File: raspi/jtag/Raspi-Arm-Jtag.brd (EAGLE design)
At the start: 67 x 36.8 mm, 2 parts

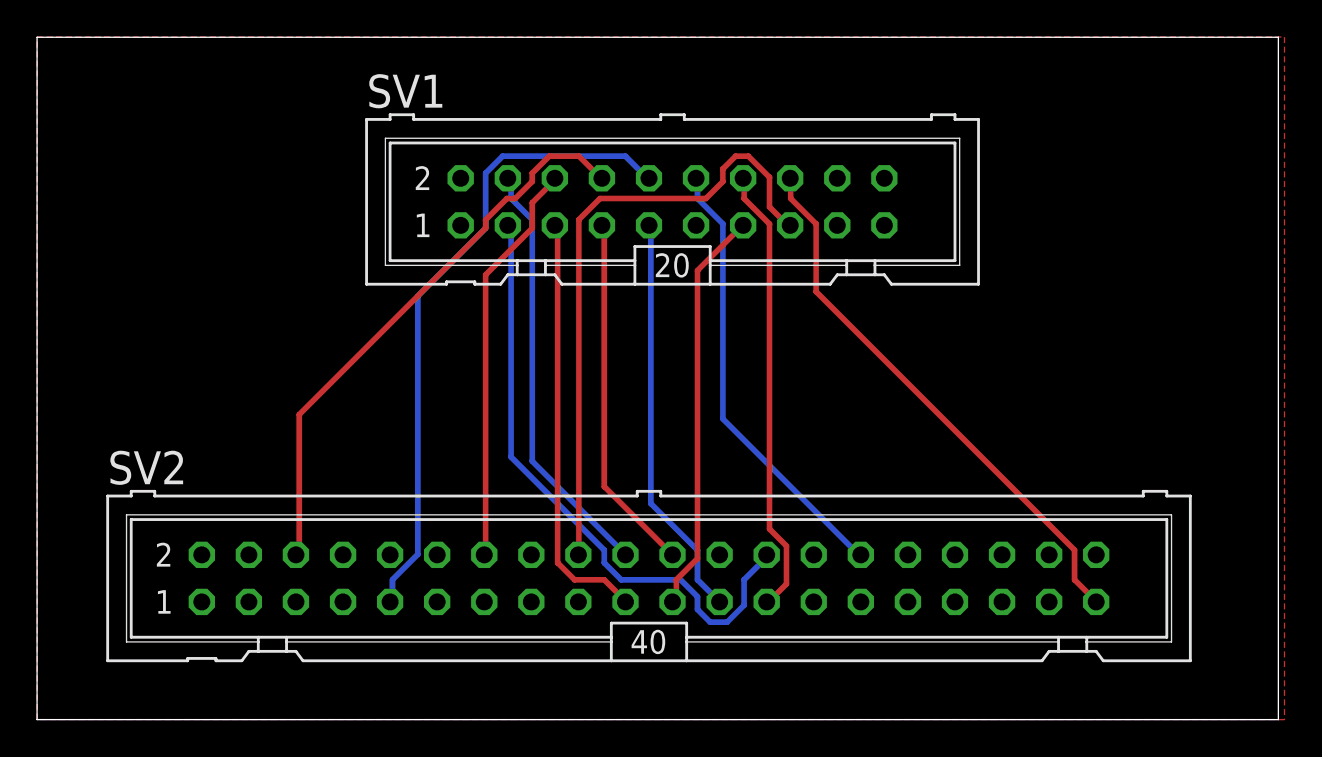
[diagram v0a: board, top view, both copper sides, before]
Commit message: Raspi: Neue Adapter-Schaltpläne
git-svn-id: https://cvsvn/svn/raspi/trunk@92 50237d99-7d21-444e-87dd-016511c29f8c
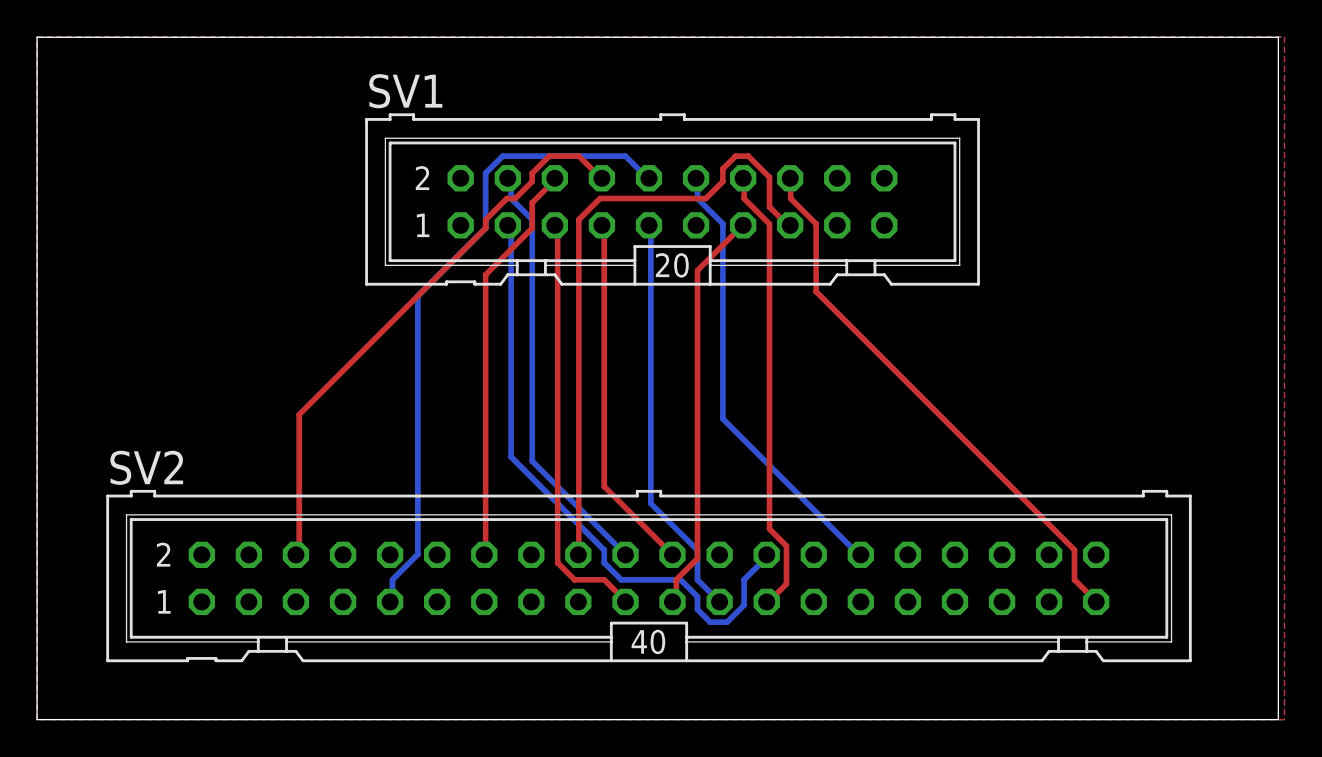
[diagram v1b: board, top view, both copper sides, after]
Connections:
- removed net N$10: SV1.4, SV2.20
- removed net N$11: SV1.10, SV2.9
- removed net N$12: SV1.14, SV2.25
- removed net N$13: SV1.16, SV2.39
- removed net N$7: SV1.6, SV2.14
- removed net N$8: SV1.8, SV2.6
- removed net N$9: SV1.12, SV2.30
- new net GND: SV1.10, SV1.12, SV1.14, SV1.16, SV1.4, SV1.6, SV1.8, SV2.14, SV2.20, SV2.25, SV2.30, SV2.39, SV2.6, SV2.9
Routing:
- net GND: track 0.00 -> 188.7 mm
- net N$11: track 35.0 -> 0.00 mm
- net N$8: track 30.9 -> 0.00 mm
- net N$13: track 29.7 -> 0.00 mm
- net N$12: track 24.3 -> 0.00 mm
- net N$9: track 24.0 -> 0.00 mm
- net N$10: track 23.0 -> 0.00 mm
- net N$7: track 21.9 -> 0.00 mm
- added copper zone on layer 1, net GND
- added copper zone on layer 16, net GND
- removed copper zone on layer 1, net GNG
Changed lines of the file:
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@@
 <wire x1="42.9768" y1="26.7462" x2="43.18" y2="26.67" width="0.3048" layer="1"/>
 </signal>
-<signal name="N$10">
-<contactref element="SV2" pad="20"/>
-<contactref element="SV1" pad="4"/>
-<wire x1="28.1178" y1="28.1178" x2="28.1178" y2="29.0322" width="0.3048" layer="16"/>
-<wire x1="29.2608" y1="26.9748" x2="28.1178" y2="28.1178" width="0.3048" layer="16"/>
-<wire x1="29.2608" y1="13.9446" x2="29.2608" y2="26.9748" width="0.3048" layer="16"/>
-<wire x1="34.29" y1="8.9154" x2="29.2608" y2="13.9446" width="0.3048" layer="16"/>
-<wire x1="28.1178" y1="29.0322" x2="27.94" y2="29.21" width="0.3048" layer="16"/>
-<wire x1="34.29" y1="8.9154" x2="34.29" y2="8.89" width="0.3048" layer="16"/>
-</signal>
-<signal name="N$7">
-<contactref element="SV2" pad="14"/>
-<contactref element="SV1" pad="6"/>
-<wire x1="26.7462" y1="24.003" x2="26.7462" y2="8.9154" width="0.3048" layer="1"/>
-<wire x1="29.2608" y1="26.5176" x2="26.7462" y2="24.003" width="0.3048" layer="1"/>
-<wire x1="29.2608" y1="27.8892" x2="29.2608" y2="26.5176" width="0.3048" layer="1"/>
-<wire x1="30.4038" y1="29.0322" x2="29.2608" y2="27.8892" width="0.3048" layer="1"/>
-<wire x1="26.7462" y1="8.9154" x2="26.67" y2="8.89" width="0.3048" layer="1"/>
-<wire x1="30.4038" y1="29.0322" x2="30.48" y2="29.21" width="0.3048" layer="1"/>
-</signal>
-<signal name="N$8">
+<signal name="GND">
+<polygon width="0.1524" layer="1" isolate="0.8128">
+<vertex x="2.54" y="36.83"/>
+<vertex x="69.85" y="36.83"/>
+<vertex x="69.85" y="0"/>
+<vertex x="2.54" y="0"/>
+</polygon>
+<contactref element="SV2" pad="25"/>
+<contactref element="SV1" pad="14"/>
+<wire x1="40.6908" y1="28.1178" x2="40.6908" y2="29.0322" width="0.3048" layer="1"/>
+<wire x1="42.0624" y1="26.7462" x2="40.6908" y2="28.1178" width="0.3048" layer="1"/>
+<wire x1="42.0624" y1="10.287" x2="42.0624" y2="26.7462" width="0.3048" layer="1"/>
+<wire x1="42.9768" y1="9.3726" x2="42.0624" y2="10.287" width="0.3048" layer="1"/>
+<wire x1="42.9768" y1="7.3152" x2="42.9768" y2="9.3726" width="0.3048" layer="1"/>
+<wire x1="42.0624" y1="6.4008" x2="42.9768" y2="7.3152" width="0.3048" layer="1"/>
+<wire x1="40.6908" y1="29.0322" x2="40.64" y2="29.21" width="0.3048" layer="1"/>
+<wire x1="42.0624" y1="6.4008" x2="41.91" y2="6.35" width="0.3048" layer="1"/>
+<contactref element="SV2" pad="30"/>
+<contactref element="SV1" pad="12"/>
+<wire x1="38.1762" y1="28.1178" x2="38.1762" y2="29.0322" width="0.3048" layer="16"/>
+<wire x1="39.5478" y1="26.7462" x2="38.1762" y2="28.1178" width="0.3048" layer="16"/>
+<wire x1="39.5478" y1="16.2306" x2="39.5478" y2="26.7462" width="0.3048" layer="16"/>
+<wire x1="46.863" y1="8.9154" x2="39.5478" y2="16.2306" width="0.3048" layer="16"/>
+<wire x1="38.1762" y1="29.0322" x2="38.1" y2="29.21" width="0.3048" layer="16"/>
+<wire x1="46.863" y1="8.9154" x2="46.99" y2="8.89" width="0.3048" layer="16"/>
+<contactref element="SV2" pad="39"/>
+<contactref element="SV1" pad="16"/>
+<wire x1="43.2054" y1="28.1178" x2="43.2054" y2="29.0322" width="0.3048" layer="1"/>
+<wire x1="44.577" y1="26.7462" x2="43.2054" y2="28.1178" width="0.3048" layer="1"/>
+<wire x1="44.577" y1="23.0886" x2="44.577" y2="26.7462" width="0.3048" layer="1"/>
+<wire x1="58.5216" y1="9.144" x2="44.577" y2="23.0886" width="0.3048" layer="1"/>
+<wire x1="58.5216" y1="7.5438" x2="58.5216" y2="9.144" width="0.3048" layer="1"/>
+<wire x1="59.6646" y1="6.4008" x2="58.5216" y2="7.5438" width="0.3048" layer="1"/>
+<wire x1="43.2054" y1="29.0322" x2="43.18" y2="29.21" width="0.3048" layer="1"/>
+<wire x1="59.6646" y1="6.4008" x2="59.69" y2="6.35" width="0.3048" layer="1"/>
+<contactref element="SV2" pad="9"/>
+<contactref element="SV1" pad="10"/>
+<wire x1="21.717" y1="7.5438" x2="21.717" y2="6.4008" width="0.3048" layer="16"/>
+<wire x1="23.0886" y1="8.9154" x2="21.717" y2="7.5438" width="0.3048" layer="16"/>
+<wire x1="23.0886" y1="22.86" x2="23.0886" y2="8.9154" width="0.3048" layer="16"/>
+<wire x1="26.7462" y1="26.5176" x2="23.0886" y2="22.86" width="0.3048" layer="16"/>
+<wire x1="26.7462" y1="29.4894" x2="26.7462" y2="26.5176" width="0.3048" layer="16"/>
+<wire x1="27.6606" y1="30.4038" x2="26.7462" y2="29.4894" width="0.3048" layer="16"/>
+<wire x1="34.29" y1="30.4038" x2="27.6606" y2="30.4038" width="0.3048" layer="16"/>
+<wire x1="35.433" y1="29.2608" x2="34.29" y2="30.4038" width="0.3048" layer="16"/>
+<wire x1="21.717" y1="6.4008" x2="21.59" y2="6.35" width="0.3048" layer="16"/>
+<wire x1="35.433" y1="29.2608" x2="35.56" y2="29.21" width="0.3048" layer="16"/>
 <contactref element="SV2" pad="6"/>
 <contactref element="SV1" pad="8"/>
@@
 <wire x1="16.6878" y1="8.9154" x2="16.51" y2="8.89" width="0.3048" layer="1"/>
 <wire x1="32.9184" y1="29.2608" x2="33.02" y2="29.21" width="0.3048" layer="1"/>
-</signal>
-<signal name="N$9">
-<contactref element="SV2" pad="30"/>
-<contactref element="SV1" pad="12"/>
-<wire x1="38.1762" y1="28.1178" x2="38.1762" y2="29.0322" width="0.3048" layer="16"/>
-<wire x1="39.5478" y1="26.7462" x2="38.1762" y2="28.1178" width="0.3048" layer="16"/>
-<wire x1="39.5478" y1="16.2306" x2="39.5478" y2="26.7462" width="0.3048" layer="16"/>
-<wire x1="46.863" y1="8.9154" x2="39.5478" y2="16.2306" width="0.3048" layer="16"/>
-<wire x1="38.1762" y1="29.0322" x2="38.1" y2="29.21" width="0.3048" layer="16"/>
-<wire x1="46.863" y1="8.9154" x2="46.99" y2="8.89" width="0.3048" layer="16"/>
-</signal>
-<signal name="N$11">
-<contactref element="SV2" pad="9"/>
-<contactref element="SV1" pad="10"/>
-<wire x1="21.717" y1="7.5438" x2="21.717" y2="6.4008" width="0.3048" layer="16"/>
-<wire x1="23.0886" y1="8.9154" x2="21.717" y2="7.5438" width="0.3048" layer="16"/>
-<wire x1="23.0886" y1="22.86" x2="23.0886" y2="8.9154" width="0.3048" layer="16"/>
-<wire x1="26.7462" y1="26.5176" x2="23.0886" y2="22.86" width="0.3048" layer="16"/>
-<wire x1="26.7462" y1="29.4894" x2="26.7462" y2="26.5176" width="0.3048" layer="16"/>
-<wire x1="27.6606" y1="30.4038" x2="26.7462" y2="29.4894" width="0.3048" layer="16"/>
-<wire x1="34.29" y1="30.4038" x2="27.6606" y2="30.4038" width="0.3048" layer="16"/>
-<wire x1="35.433" y1="29.2608" x2="34.29" y2="30.4038" width="0.3048" layer="16"/>
-<wire x1="21.717" y1="6.4008" x2="21.59" y2="6.35" width="0.3048" layer="16"/>
-<wire x1="35.433" y1="29.2608" x2="35.56" y2="29.21" width="0.3048" layer="16"/>
-</signal>
-<signal name="N$12">
-<contactref element="SV2" pad="25"/>
-<contactref element="SV1" pad="14"/>
-<wire x1="40.6908" y1="28.1178" x2="40.6908" y2="29.0322" width="0.3048" layer="1"/>
-<wire x1="42.0624" y1="26.7462" x2="40.6908" y2="28.1178" width="0.3048" layer="1"/>
-<wire x1="42.0624" y1="10.287" x2="42.0624" y2="26.7462" width="0.3048" layer="1"/>
-<wire x1="42.9768" y1="9.3726" x2="42.0624" y2="10.287" width="0.3048" layer="1"/>
-<wire x1="42.9768" y1="7.3152" x2="42.9768" y2="9.3726" width="0.3048" layer="1"/>
-<wire x1="42.0624" y1="6.4008" x2="42.9768" y2="7.3152" width="0.3048" layer="1"/>
-<wire x1="40.6908" y1="29.0322" x2="40.64" y2="29.21" width="0.3048" layer="1"/>
-<wire x1="42.0624" y1="6.4008" x2="41.91" y2="6.35" width="0.3048" layer="1"/>
-</signal>
-<signal name="N$13">
-<contactref element="SV2" pad="39"/>
-<contactref element="SV1" pad="16"/>
-<wire x1="43.2054" y1="28.1178" x2="43.2054" y2="29.0322" width="0.3048" layer="1"/>
-<wire x1="44.577" y1="26.7462" x2="43.2054" y2="28.1178" width="0.3048" layer="1"/>
-<wire x1="44.577" y1="23.0886" x2="44.577" y2="26.7462" width="0.3048" layer="1"/>
-<wire x1="58.5216" y1="9.144" x2="44.577" y2="23.0886" width="0.3048" layer="1"/>
-<wire x1="58.5216" y1="7.5438" x2="58.5216" y2="9.144" width="0.3048" layer="1"/>
-<wire x1="59.6646" y1="6.4008" x2="58.5216" y2="7.5438" width="0.3048" layer="1"/>
-<wire x1="43.2054" y1="29.0322" x2="43.18" y2="29.21" width="0.3048" layer="1"/>
-<wire x1="59.6646" y1="6.4008" x2="59.69" y2="6.35" width="0.3048" layer="1"/>
-</signal>
-<signal name="GNG">
-<polygon width="0.3048" layer="1">
+<contactref element="SV2" pad="14"/>
+<contactref element="SV1" pad="6"/>
+<wire x1="26.7462" y1="24.003" x2="26.7462" y2="8.9154" width="0.3048" layer="1"/>
+<wire x1="29.2608" y1="26.5176" x2="26.7462" y2="24.003" width="0.3048" layer="1"/>
+<wire x1="29.2608" y1="27.8892" x2="29.2608" y2="26.5176" width="0.3048" layer="1"/>
+<wire x1="30.4038" y1="29.0322" x2="29.2608" y2="27.8892" width="0.3048" layer="1"/>
+<wire x1="26.7462" y1="8.9154" x2="26.67" y2="8.89" width="0.3048" layer="1"/>
+<wire x1="30.4038" y1="29.0322" x2="30.48" y2="29.21" width="0.3048" layer="1"/>
+<contactref element="SV2" pad="20"/>
+<contactref element="SV1" pad="4"/>
+<wire x1="28.1178" y1="28.1178" x2="28.1178" y2="29.0322" width="0.3048" layer="16"/>
+<wire x1="29.2608" y1="26.9748" x2="28.1178" y2="28.1178" width="0.3048" layer="16"/>
+<wire x1="29.2608" y1="13.9446" x2="29.2608" y2="26.9748" width="0.3048" layer="16"/>
+<wire x1="34.29" y1="8.9154" x2="29.2608" y2="13.9446" width="0.3048" layer="16"/>
+<wire x1="28.1178" y1="29.0322" x2="27.94" y2="29.21" width="0.3048" layer="16"/>
+<wire x1="34.29" y1="8.9154" x2="34.29" y2="8.89" width="0.3048" layer="16"/>
+<polygon width="0.1524" layer="16" isolate="0.6096">
 <vertex x="2.54" y="36.83"/>
 <vertex x="69.85" y="36.83"/>
